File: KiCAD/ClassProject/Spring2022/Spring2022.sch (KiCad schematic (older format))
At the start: 0 parts

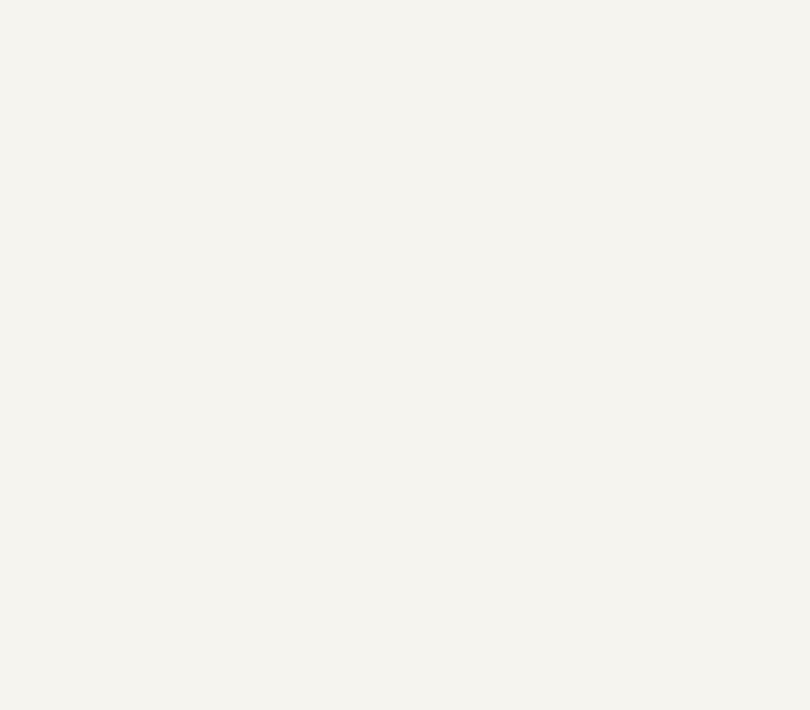
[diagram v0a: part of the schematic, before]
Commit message: Added Fub Mini Sch Symbol and added to schematic.
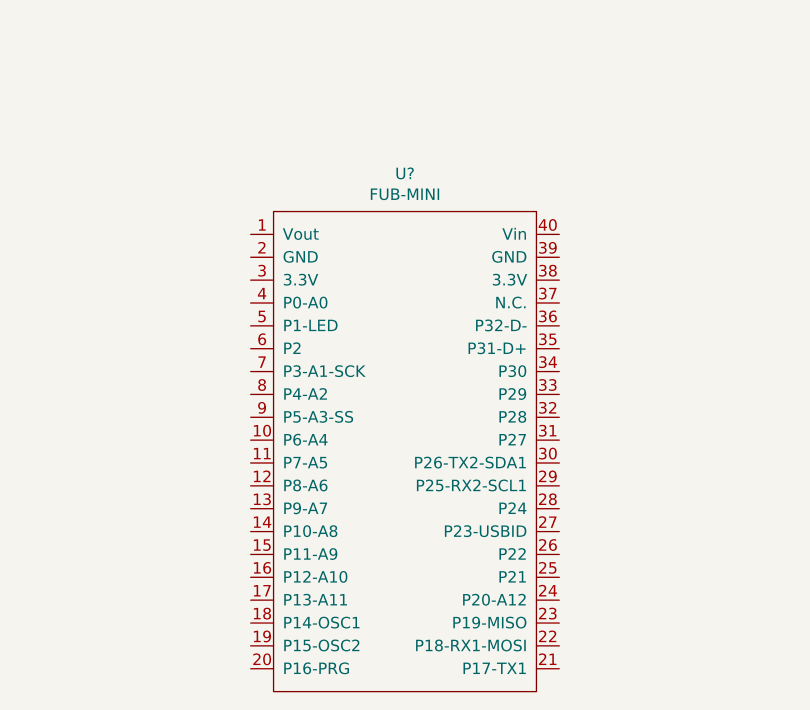
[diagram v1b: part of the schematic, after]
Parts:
- added U?: FUB-MINI, 74_Patrick B:FubSocket_DIP-40_600_ELL, symbol 74_Patrick:FUB-MINI
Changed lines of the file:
@@
 F5 "~LED-OE" I R 2700 3050 50
 $EndSheet
+$Comp
+L 74_Patrick:FUB-MINI U?
+U 1 1 625BD726
+P 3800 5650
+F 0 "U?" H 3775 6715 50  0000 C CNN
+F 1 "FUB-MINI" H 3775 6624 50  0000 C CNN
+F 2 "74_Patrick B:FubSocket_DIP-40_600_ELL" H 3600 5650 50  0001 C CNN
+F 3 "" H 3600 5650 50  0001 C CNN
+	1    3800 5650
+	1    0    0    -1
+$EndComp
 $EndSCHEMATC

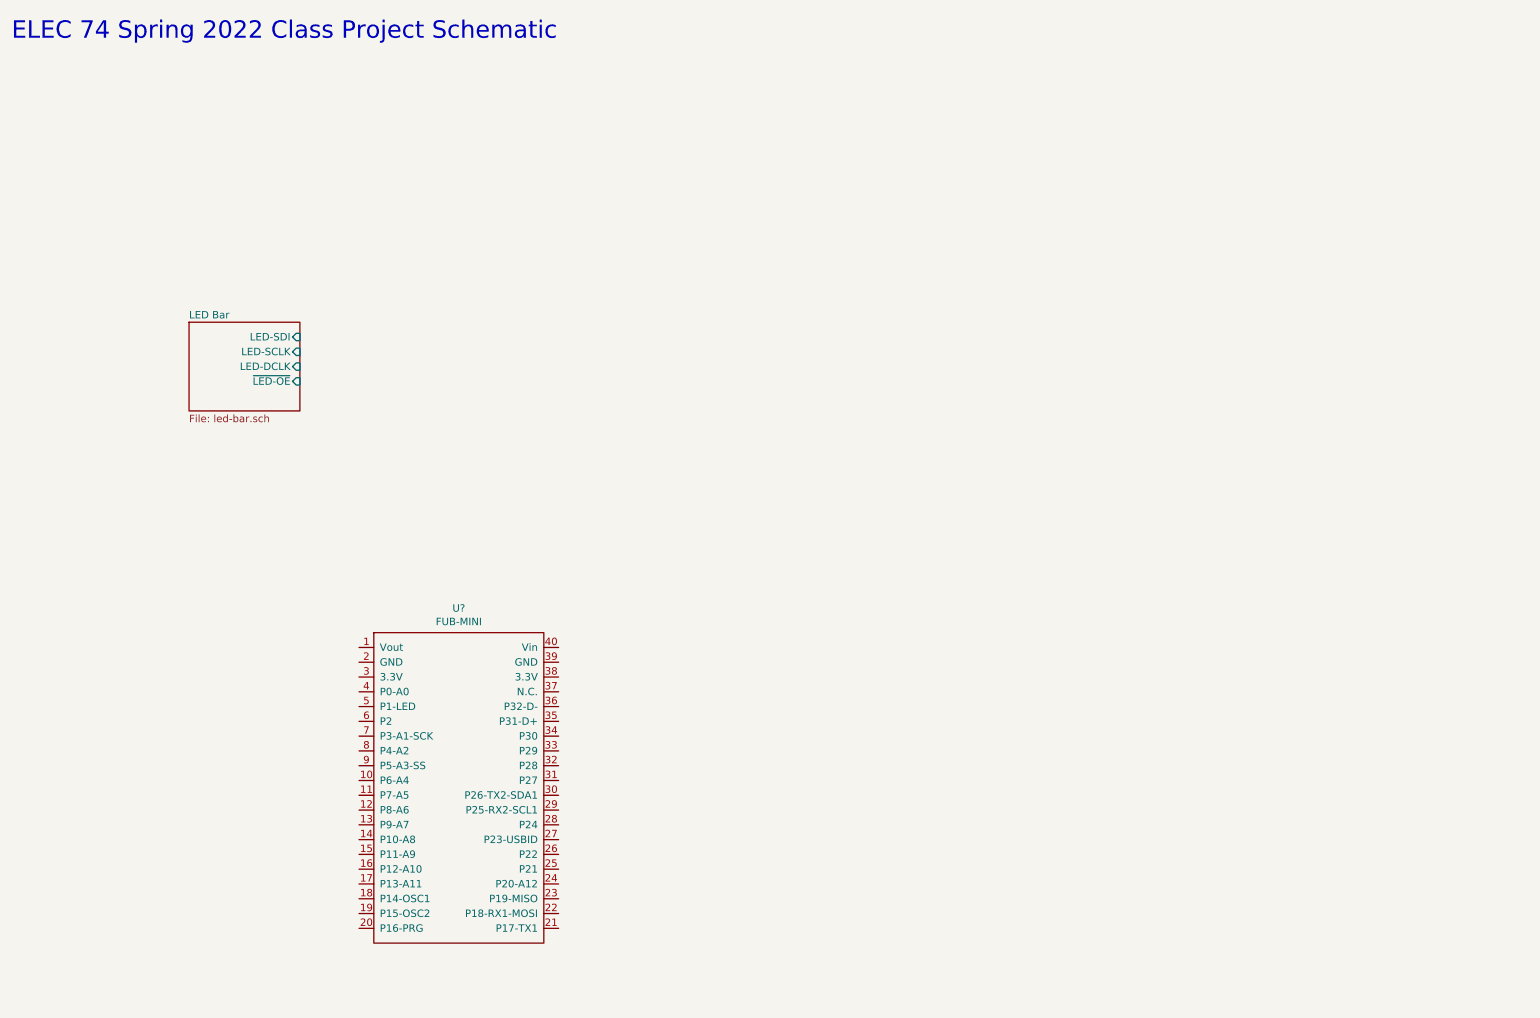
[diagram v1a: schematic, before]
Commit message: Added Battery Holder
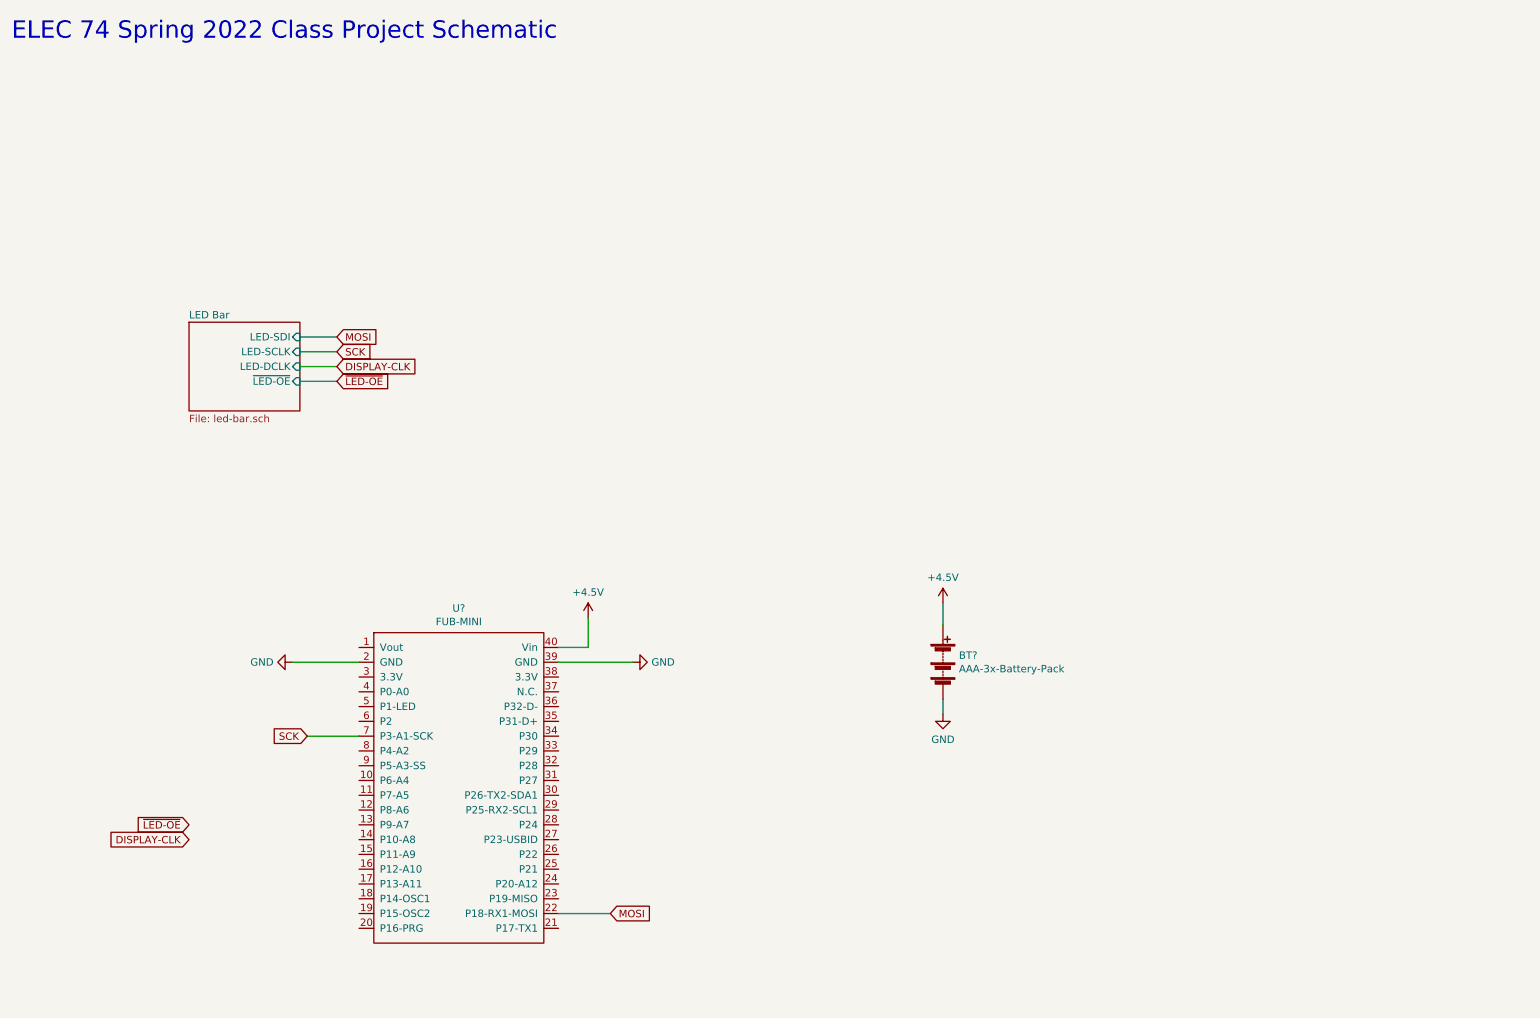
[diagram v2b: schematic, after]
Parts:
- added BT?: AAA-3x-Battery-Pack, 74_jacob:BatteryHolder_Keystone_2479_3xAAA, symbol 74_Jacob:AAA-3x-Battery-Pack
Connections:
- net GND: now reaches U?.2 (GND)
- net GND: now also U?.39 (GND), BT?.2 (-)
- net MOSI: now reaches U?.22 (P18-RX1-MOSI)
- net +4V: now reaches U?.40 (Vin)
- net +4V: now also BT?.1 (+)
- net SCK: now reaches U?.7 (P3-A1-SCK)
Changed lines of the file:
@@
 	1    0    0    -1
 $EndComp
+$Comp
+L 74_Jacob:AAA-3x-Battery-Pack BT?
+U 1 1 625D9A46
+P 7050 4950
+F 0 "BT?" H 7158 4996 50  0000 L CNN
+F 1 "AAA-3x-Battery-Pack" H 7158 4905 50  0000 L CNN
+F 2 "74_jacob:BatteryHolder_Keystone_2479_3xAAA" V 7050 5060 50  0001 C CNN
+F 3 "~" V 7050 5060 50  0001 C CNN
+	1    7050 4950
+	1    0    0    -1
+$EndComp
+Wire Wire Line
+	7050 5200 7050 5300
+$Comp
+L 74_Jacob:+4.5V #PWR?
+U 1 1 625DDEA1
+P 7050 4550
+F 0 "#PWR?" H 7050 4400 50  0001 C CNN
+F 1 "+4.5V" H 7050 4723 50  0000 C CNN
+F 2 "" H 7050 4550 50  0001 C CNN
+F 3 "" H 7050 4550 50  0001 C CNN
+	1    7050 4550
+	1    0    0    -1
+$EndComp
+Wire Wire Line
+	7050 4550 7050 4700
+$Comp
+L 74_Jacob:+4.5V #PWR?
+U 1 1 625DE893
+P 4650 4650
+F 0 "#PWR?" H 4650 4500 50  0001 C CNN
+F 1 "+4.5V" H 4650 4823 50  0000 C CNN
+F 2 "" H 4650 4650 50  0001 C CNN
+F 3 "" H 4650 4650 50  0001 C CNN
+	1    4650 4650
+	1    0    0    -1
+$EndComp
+Wire Wire Line
+	4650 4650 4650 4850
+Wire Wire Line
+	4650 4850 4450 4850
+$Comp
+L 74_Jacob:GND #PWR?
+U 1 1 625DF7B3
+P 7050 5300
+F 0 "#PWR?" H 7050 5050 50  0001 C CNN
+F 1 "GND" H 7050 5127 50  0000 C CNN
+F 2 "" H 7050 5300 50  0001 C CNN
+F 3 "" H 7050 5300 50  0001 C CNN
+	1    7050 5300
+	1    0    0    -1
+$EndComp
+$Comp
+L 74_Jacob:GND #PWR?
+U 1 1 625DFDFE
+P 4950 4950
+F 0 "#PWR?" H 4950 4700 50  0001 C CNN
+F 1 "GND" V 4950 4822 50  0000 R CNN
+F 2 "" H 4950 4950 50  0001 C CNN
+F 3 "" H 4950 4950 50  0001 C CNN
+	1    4950 4950
+	0    -1   -1   0
+$EndComp
+Wire Wire Line
+	4950 4950 4450 4950
+$Comp
+L 74_Jacob:GND #PWR?
+U 1 1 625E0E59
+P 2650 4950
+F 0 "#PWR?" H 2650 4700 50  0001 C CNN
+F 1 "GND" V 2650 4822 50  0000 R CNN
+F 2 "" H 2650 4950 50  0001 C CNN
+F 3 "" H 2650 4950 50  0001 C CNN
+	1    2650 4950
+	0    1    1    0
+$EndComp
+Wire Wire Line
+	2650 4950 3100 4950
+Text GLabel 4800 6650 2    50   Input ~ 0
+MOSI
+Wire Wire Line
+	4800 6650 4450 6650
+Text GLabel 2950 2750 2    50   Input ~ 0
+MOSI
+Wire Wire Line
+	2950 2750 2700 2750
+Text GLabel 2950 2850 2    50   Input ~ 0
+SCK
+Wire Wire Line
+	2950 2850 2700 2850
+Text GLabel 2750 5450 0    50   Input ~ 0
+SCK
+Wire Wire Line
+	2750 5450 3100 5450
+Text GLabel 2950 2950 2    50   Input ~ 0
+DISPLAY-CLK
+Text GLabel 2950 3050 2    50   Input ~ 0
+~LED-OE
+Wire Wire Line
+	2950 3050 2700 3050
+Wire Wire Line
+	2700 2950 2950 2950
+Text GLabel 1950 6150 0    50   Input ~ 0
+DISPLAY-CLK
+Text GLabel 1950 6050 0    50   Input ~ 0
+~LED-OE
 $EndSCHEMATC

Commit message: Setup PCB and Annotated Parts
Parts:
- removed BT?: AAA-3x-Battery-Pack, 74_jacob:BatteryHolder_Keystone_2479_3xAAA, symbol 74_Jacob:AAA-3x-Battery-Pack
- added BT1: AAA-3x-Battery-Pack, 74_jacob:BatteryHolder_Keystone_2479_3xAAA, symbol 74_Jacob:AAA-3x-Battery-Pack
- gave numbers to parts that had none: 1
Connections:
- net +4V: now also BT1.1 (+)
- net GND: now also BT1.2 (-)
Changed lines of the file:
@@
 $EndSheet
 $Comp
-L 74_Patrick:FUB-MINI U?
+L 74_Patrick:FUB-MINI U1
 U 1 1 625BD726
 P 3800 5650
-F 0 "U?" H 3775 6715 50  0000 C CNN
+F 0 "U1" H 3775 6715 50  0000 C CNN
 F 1 "FUB-MINI" H 3775 6624 50  0000 C CNN
 F 2 "74_Patrick B:FubSocket_DIP-40_600_ELL" H 3600 5650 50  0001 C CNN
@@
 	1    0    0    -1
 $EndComp
-$Comp
-L 74_Jacob:AAA-3x-Battery-Pack BT?
-U 1 1 625D9A46
-P 7050 4950
-F 0 "BT?" H 7158 4996 50  0000 L CNN
-F 1 "AAA-3x-Battery-Pack" H 7158 4905 50  0000 L CNN
-F 2 "74_jacob:BatteryHolder_Keystone_2479_3xAAA" V 7050 5060 50  0001 C CNN
-F 3 "~" V 7050 5060 50  0001 C CNN
-	1    7050 4950
-	1    0    0    -1
-$EndComp
 Wire Wire Line
 	7050 5200 7050 5300
 $Comp
-L 74_Jacob:+4.5V #PWR?
+L 74_Jacob:+4.5V #PWR0101
 U 1 1 625DDEA1
 P 7050 4550
-F 0 "#PWR?" H 7050 4400 50  0001 C CNN
+F 0 "#PWR0101" H 7050 4400 50  0001 C CNN
 F 1 "+4.5V" H 7050 4723 50  0000 C CNN
 F 2 "" H 7050 4550 50  0001 C CNN
@@
 	7050 4550 7050 4700
 $Comp
-L 74_Jacob:+4.5V #PWR?
+L 74_Jacob:+4.5V #PWR0104
 U 1 1 625DE893
 P 4650 4650
-F 0 "#PWR?" H 4650 4500 50  0001 C CNN
+F 0 "#PWR0104" H 4650 4500 50  0001 C CNN
 F 1 "+4.5V" H 4650 4823 50  0000 C CNN
 F 2 "" H 4650 4650 50  0001 C CNN
@@
 	4650 4850 4450 4850
 $Comp
-L 74_Jacob:GND #PWR?
+L 74_Jacob:GND #PWR0105
 U 1 1 625DF7B3
 P 7050 5300
-F 0 "#PWR?" H 7050 5050 50  0001 C CNN
+F 0 "#PWR0105" H 7050 5050 50  0001 C CNN
 F 1 "GND" H 7050 5127 50  0000 C CNN
 F 2 "" H 7050 5300 50  0001 C CNN
@@
 $EndComp
 $Comp
-L 74_Jacob:GND #PWR?
+L 74_Jacob:GND #PWR0106
 U 1 1 625DFDFE
 P 4950 4950
-F 0 "#PWR?" H 4950 4700 50  0001 C CNN
+F 0 "#PWR0106" H 4950 4700 50  0001 C CNN
 F 1 "GND" V 4950 4822 50  0000 R CNN
 F 2 "" H 4950 4950 50  0001 C CNN
@@
 	4950 4950 4450 4950
 $Comp
-L 74_Jacob:GND #PWR?
+L 74_Jacob:GND #PWR0107
 U 1 1 625E0E59
 P 2650 4950
-F 0 "#PWR?" H 2650 4700 50  0001 C CNN
+F 0 "#PWR0107" H 2650 4700 50  0001 C CNN
 F 1 "GND" V 2650 4822 50  0000 R CNN
 F 2 "" H 2650 4950 50  0001 C CNN
@@
 Text GLabel 1950 6050 0    50   Input ~ 0
 ~LED-OE
+$Comp
+L 74_Jacob:AAA-3x-Battery-Pack BT1
+U 1 1 625CF271
+P 7050 4950
+F 0 "BT1" H 7158 4996 50  0000 L CNN
+F 1 "AAA-3x-Battery-Pack" H 7158 4905 50  0000 L CNN
+F 2 "74_jacob:BatteryHolder_Keystone_2479_3xAAA" V 7050 5060 50  0001 C CNN
+F 3 "~" V 7050 5060 50  0001 C CNN
+	1    7050 4950
+	1    0    0    -1
+$EndComp
 $EndSCHEMATC
